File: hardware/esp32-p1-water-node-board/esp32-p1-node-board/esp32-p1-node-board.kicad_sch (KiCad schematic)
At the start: 17 parts, among them J1 RJ11-6, Q1 BC847, Q2 BSS138, U1 TTGO_LoRa32_V11

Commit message: update
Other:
- note added: "GPIO4 zal gebruikt worden als RTS voor de slimmeter"
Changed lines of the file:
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@@
+    (effects (font (size 1.27 1.27)) (justify left bottom))
+  )
+  (text "GPIO4 zal gebruikt worden als RTS voor de slimmeter"
+    (at 208.407 92.583 0)
     (effects (font (size 1.27 1.27)) (justify left bottom))
   )
@@
     (effects (font (size 1.27 1.27)) (justify right bottom))
   )
-  (label "DATA_REQ" (at 40.64 36.83 0)
+  (label "DATA_REQ" (at 40.64 36.83 0) (fields_autoplaced)
     (effects (font (size 1.27 1.27)) (justify left bottom))
   )
-  (label "3V3" (at 111.76 58.42 0)
+  (label "3V3" (at 111.76 58.42 0) (fields_autoplaced)
     (effects (font (size 1.27 1.27)) (justify left bottom))
   )
-  (label "3V3" (at 161.29 58.42 0)
+  (label "3V3" (at 161.29 58.42 0) (fields_autoplaced)
     (effects (font (size 1.27 1.27)) (justify left bottom))
   )
-  (label "3V3" (at 105.41 137.16 180)
+  (label "3V3" (at 105.41 137.16 180) (fields_autoplaced)
     (effects (font (size 1.27 1.27)) (justify right bottom))
   )
-  (label "3V3" (at 59.69 140.97 180)
+  (label "3V3" (at 59.69 140.97 180) (fields_autoplaced)
     (effects (font (size 1.27 1.27)) (justify right bottom))
   )
-  (label "5V" (at 36.83 54.61 0)
+  (label "5V" (at 36.83 54.61 0) (fields_autoplaced)
     (effects (font (size 1.27 1.27)) (justify left bottom))
   )
-  (label "HARD_RXD" (at 73.66 113.03 0)
+  (label "HARD_RXD" (at 73.66 113.03 0) (fields_autoplaced)
     (effects (font (size 1.27 1.27)) (justify left bottom))
   )
-  (label "HARD_RXD" (at 111.76 63.5 0)
+  (label "HARD_RXD" (at 111.76 63.5 0) (fields_autoplaced)
     (effects (font (size 1.27 1.27)) (justify left bottom))
   )
-  (label "DATA" (at 40.64 29.21 0)
+  (label "DATA" (at 40.64 29.21 0) (fields_autoplaced)
     (effects (font (size 1.27 1.27)) (justify left bottom))
   )
-  (label "SOFT_REQ" (at 73.66 137.16 0)
+  (label "SOFT_REQ" (at 73.66 137.16 0) (fields_autoplaced)
     (effects (font (size 1.27 1.27)) (justify left bottom))
   )
-  (label "GND" (at 161.29 53.34 0)
+  (label "GND" (at 161.29 53.34 0) (fields_autoplaced)
     (effects (font (size 1.27 1.27)) (justify left bottom))
   )
-  (label "DATA_GND" (at 40.64 34.29 0)
+  (label "DATA_GND" (at 40.64 34.29 0) (fields_autoplaced)
     (effects (font (size 1.27 1.27)) (justify left bottom))
   )
-  (label "DATA_3V3" (at 105.41 168.91 180)
+  (label "DATA_3V3" (at 105.41 168.91 180) (fields_autoplaced)
     (effects (font (size 1.27 1.27)) (justify right bottom))
   )
-  (label "GND" (at 165.1 138.43 180)
+  (label "GND" (at 165.1 138.43 180) (fields_autoplaced)
     (effects (font (size 1.27 1.27)) (justify right bottom))
   )
-  (label "5V" (at 161.29 55.88 0)
+  (label "5V" (at 161.29 55.88 0) (fields_autoplaced)
     (effects (font (size 1.27 1.27)) (justify left bottom))
   )
-  (label "SOFT_RXD" (at 156.21 73.66 0)
+  (label "SOFT_RXD" (at 156.21 73.66 0) (fields_autoplaced)
     (effects (font (size 1.27 1.27)) (justify left bottom))
   )
-  (label "3V3" (at 77.47 54.61 0)
+  (label "3V3" (at 77.47 54.61 0) (fields_autoplaced)
     (effects (font (size 1.27 1.27)) (justify left bottom))
   )
-  (label "5V" (at 111.76 55.88 0)
+  (label "5V" (at 111.76 55.88 0) (fields_autoplaced)
     (effects (font (size 1.27 1.27)) (justify left bottom))
   )
-  (label "SOFT_REQ" (at 165.1 81.28 180)
+  (label "SOFT_REQ" (at 165.1 81.28 180) (fields_autoplaced)
     (effects (font (size 1.27 1.27)) (justify right bottom))
   )
-  (label "DATA_3V3_N" (at 105.41 161.29 180)
+  (label "DATA_3V3_N" (at 105.41 161.29 180) (fields_autoplaced)
     (effects (font (size 1.27 1.27)) (justify right bottom))
   )
-  (label "SDA" (at 161.29 96.52 0)
+  (label "SDA" (at 161.29 96.52 0) (fields_autoplaced)
     (effects (font (size 1.27 1.27)) (justify left bottom))
   )
-  (label "DATA_3V3_N" (at 83.82 67.31 0)
+  (label "DATA_3V3_N" (at 83.82 67.31 0) (fields_autoplaced)
     (effects (font (size 1.27 1.27)) (justify left bottom))
   )
-  (label "SOFT_TXD" (at 165.1 71.12 180)
+  (label "SOFT_TXD" (at 165.1 71.12 180) (fields_autoplaced)
     (effects (font (size 1.27 1.27)) (justify right bottom))
   )
-  (label "GND" (at 111.76 60.96 0)
+  (label "GND" (at 111.76 60.96 0) (fields_autoplaced)
     (effects (font (size 1.27 1.27)) (justify left bottom))
   )
-  (label "5V" (at 165.1 128.27 180)
+  (label "5V" (at 165.1 128.27 180) (fields_autoplaced)
     (effects (font (size 1.27 1.27)) (justify right bottom))
   )
-  (label "DATA_GND" (at 26.67 87.63 0)
+  (label "DATA_GND" (at 26.67 87.63 0) (fields_autoplaced)
     (effects (font (size 1.27 1.27)) (justify left bottom))
   )
-  (label "DATA_5V_R" (at 38.1 161.29 180)
+  (label "DATA_5V_R" (at 38.1 161.29 180) (fields_autoplaced)
     (effects (font (size 1.27 1.27)) (justify right bottom))
   )
-  (label "SOFT_RXD" (at 105.41 113.03 180)
+  (label "SOFT_RXD" (at 105.41 113.03 180) (fields_autoplaced)
     (effects (font (size 1.27 1.27)) (justify right bottom))
   )
-  (label "DATA_REQ" (at 105.41 144.78 180)
+  (label "DATA_REQ" (at 105.41 144.78 180) (fields_autoplaced)
     (effects (font (size 1.27 1.27)) (justify right bottom))
   )
-  (label "BUTTON" (at 111.76 71.12 0)
+  (label "BUTTON" (at 111.76 71.12 0) (fields_autoplaced)
     (effects (font (size 1.27 1.27)) (justify left bottom))
   )
-  (label "5V" (at 41.91 140.97 180)
+  (label "5V" (at 41.91 140.97 180) (fields_autoplaced)
     (effects (font (size 1.27 1.27)) (justify right bottom))
   )
-  (label "DATA" (at 26.67 73.66 0)
+  (label "DATA" (at 26.67 73.66 0) (fields_autoplaced)
     (effects (font (size 1.27 1.27)) (justify left bottom))
   )
-  (label "GND" (at 83.82 87.63 0)
+  (label "GND" (at 83.82 87.63 0) (fields_autoplaced)
     (effects (font (size 1.27 1.27)) (justify left bottom))
   )
-  (label "DATA_5V_R" (at 53.34 46.99 0)
+  (label "DATA_5V_R" (at 53.34 46.99 0) (fields_autoplaced)
     (effects (font (size 1.27 1.27)) (justify left bottom))
   )
-  (label "RESET" (at 111.76 68.58 0)
+  (label "RESET" (at 111.76 68.58 0) (fields_autoplaced)
     (effects (font (size 1.27 1.27)) (justify left bottom))
   )
-  (label "5V" (at 66.04 54.61 0)
+  (label "5V" (at 66.04 54.61 0) (fields_autoplaced)
     (effects (font (size 1.27 1.27)) (justify left bottom))
   )
-  (label "SCL" (at 111.76 73.66 0)
+  (label "SCL" (at 111.76 73.66 0) (fields_autoplaced)
     (effects (font (size 1.27 1.27)) (justify left bottom))
   )
-  (label "GND" (at 111.76 53.34 0)
+  (label "GND" (at 111.76 53.34 0) (fields_autoplaced)
     (effects (font (size 1.27 1.27)) (justify left bottom))
   )
-  (label "GND" (at 40.64 26.67 0)
+  (label "GND" (at 40.64 26.67 0) (fields_autoplaced)
     (effects (font (size 1.27 1.27)) (justify left bottom))
   )
-  (label "NC" (at 40.64 31.75 0)
+  (label "NC" (at 40.64 31.75 0) (fields_autoplaced)
     (effects (font (size 1.27 1.27)) (justify left bottom))
   )
-  (label "DATA_3V3" (at 105.41 120.65 180)
+  (label "DATA_3V3" (at 105.41 120.65 180) (fields_autoplaced)
     (effects (font (size 1.27 1.27)) (justify right bottom))
   )

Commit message: Update
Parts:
- removed C1: 10n, Capacitor_SMD:C_1206_3216Metric, symbol Device:C
- removed JP1, JP3: Serial-type-select, Jumpers:SMT-JUMPER_3_1-NC_TRACE_SILK, symbol esp32-p1-node-board-rescue:JUMPER-SMT_3_1-NC-SparkFun-Jumpers
- removed JP2: Data-request-select, Jumpers:SMT-JUMPER_3_1-NC_TRACE_SILK, symbol esp32-p1-node-board-rescue:JUMPER-SMT_3_1-NC-SparkFun-Jumpers
- removed Q1: BC847, Package_TO_SOT_SMD:SOT-23, symbol Transistor_BJT:BC847
- removed R3: 12K, Resistor_SMD:R_1206_3216Metric, symbol Device:R
- added D2: BAT54S, Package_TO_SOT_SMD:SOT-23, symbol esp32-p1-node-board-rescue:BAT54S-Diode
- added J2: Conn_01x03, symbol Connector_Generic:Conn_01x03
- added Q1: BSS138, Package_TO_SOT_SMD:SOT-23, symbol Transistor_FET:BSS138
- added U2: ~, symbol my-KiCad-library:TTGO_T3_V1.6.1
- R2: value 1K -> 10K
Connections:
- net 3V3: now also U2.11 (3V3); no longer Q2.1 (G), R5.1, U1.3 (3V3), U1.34 (3V3)
- net 5V: now also D2.2, U2.13 (5V); no longer R1.1, R4.1, U1.2 (5V), U1.35 (5V)
- net HARD_RXD: now also U2.3 (RXD); no longer U1.5 (GPIO03)
- net DATA_P1_3V3: now reaches Q2.2 (S), R5.2
- removed net DATA: J1.5, R1.2, R2.2
- net DATA_5V_R renamed DATA_P1
- net DATA_P1: now also J1.5; no longer R2.1
- removed net DATA_GND: C2.2, C3.1, Conn1.5 (GND), D1.1, J1.3, J1.6, U1.1 (GND), U1.36 (GND), U1.4 (GND)
- net DATA_REQ renamed DATA_P1_REQ
- new net: Q2.1 (G), R5.1
- new net: Q1.1 (G), R2.1
- new net DATA_P1_GND: D1.1, J1.3
- new net GND: C2.2, C3.1, Conn1.5 (GND), J1.6, U2.10 (GND), U2.12 (GND)
- new net PULSE_WATER: D2.3, Q1.3 (D), R1.2
- new net PULSE_WATER_3V3: Q1.2 (S), R2.2
- new net PULSE_WATER_GND: D2.1
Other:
- note removed: "C1 is not required"
- note removed: "LED"
- note removed: "LoRa_CS"
- note removed: "LoRa_IRQ"
- note removed: "LoRa_MISO"
- note removed: "LoRa_MOSI"
- note removed: "LoRa_RST"
- note removed: "LoRa_SCK"
- note removed: "OLED_RST"
- note removed: "OLED_SCL"
- note removed: "OLED_SDA"
- company: (none) -> IoT Apeldoorn
- title: (none) -> IoT-Apeldoorn P1/Watermeter LoRaWAN node
- moved on the sheet: C2, C3, Conn1, D1, Q2, R4, R5, U1

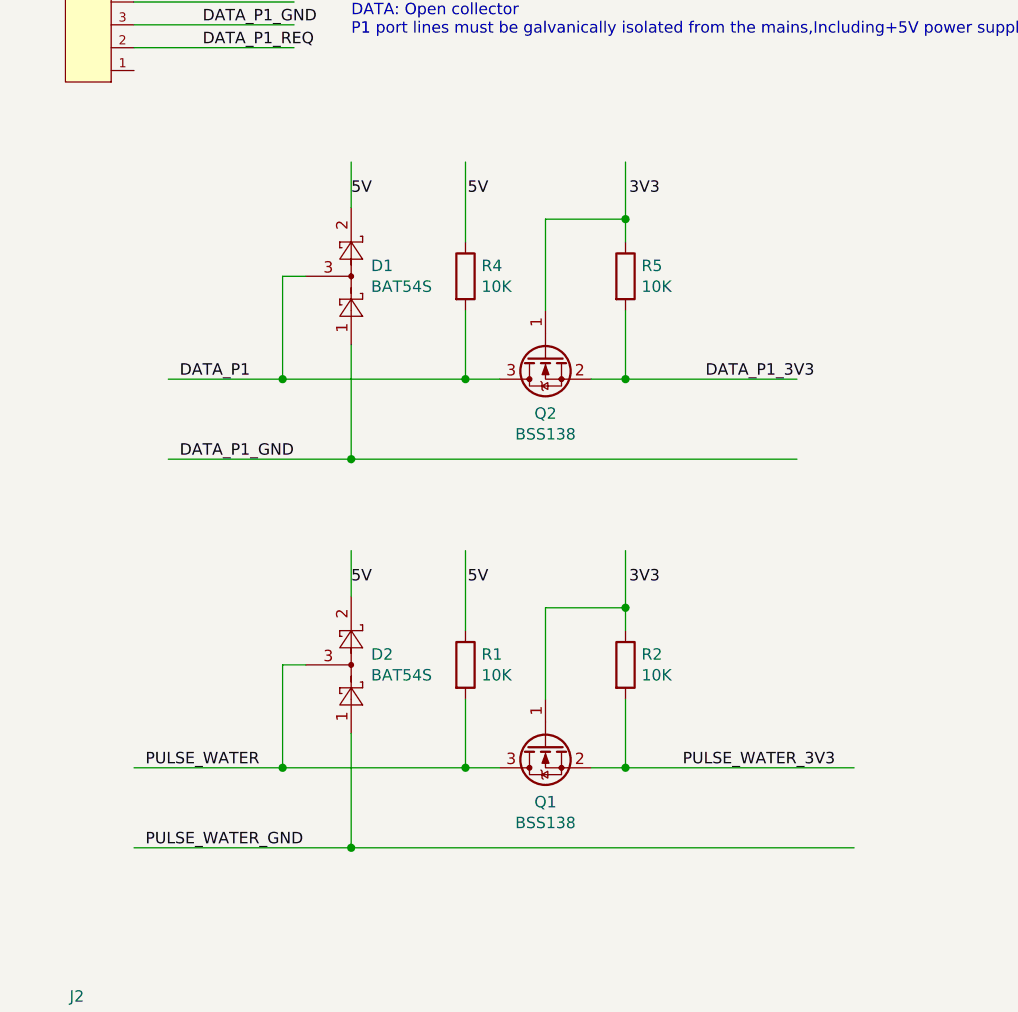
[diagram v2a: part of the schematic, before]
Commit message: Corrections on circuit
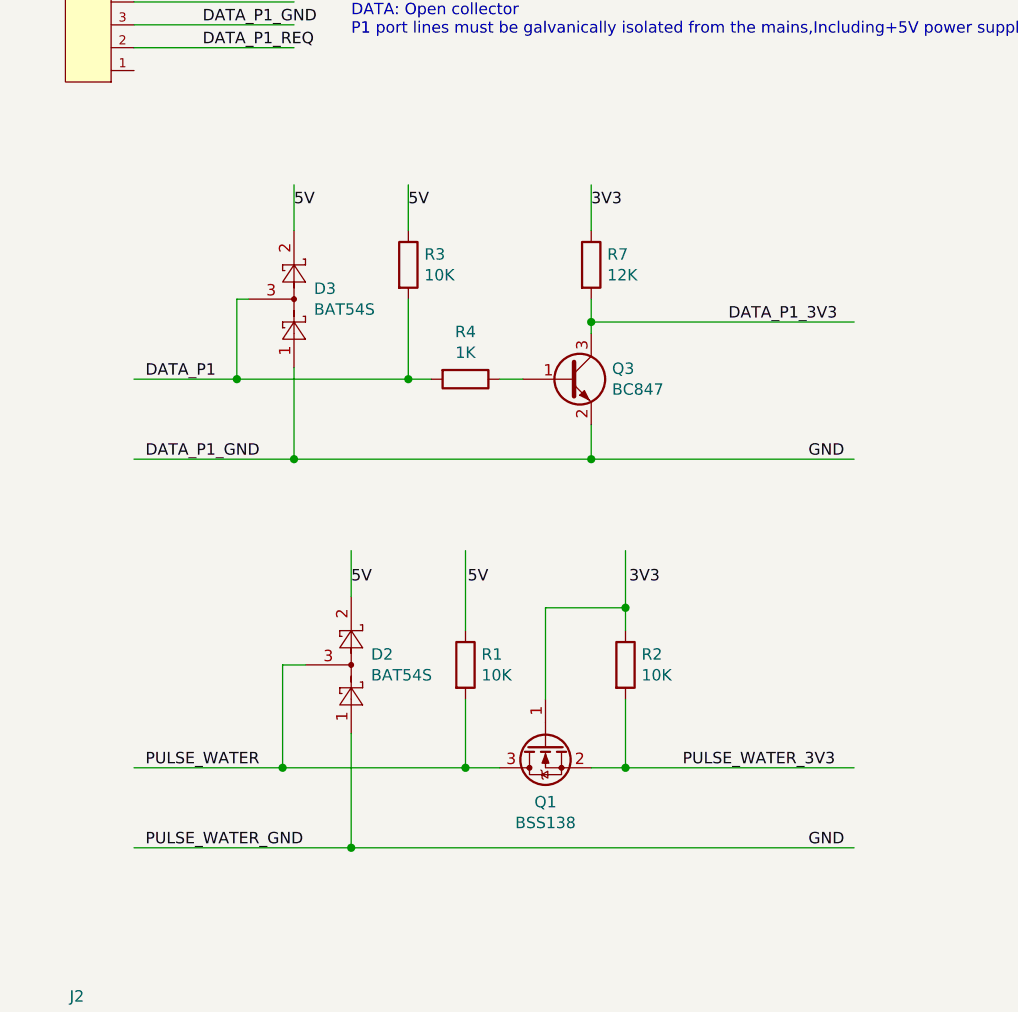
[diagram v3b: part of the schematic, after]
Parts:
- removed D1: BAT54S, Package_TO_SOT_SMD:SOT-23, symbol esp32-p1-node-board-rescue:BAT54S-Diode
- removed Q2: BSS138, Package_TO_SOT_SMD:SOT-23, symbol Transistor_FET:BSS138
- removed R5: 10K, Resistor_SMD:R_1206_3216Metric, symbol Device:R
- added D3: BAT54S, Package_TO_SOT_SMD:SOT-23, symbol esp32-p1-node-board-rescue:BAT54S-Diode
- added Q3: BC847, Package_TO_SOT_SMD:SOT-23, symbol Transistor_BJT:BC847
- added R3: 10K, Resistor_SMD:R_1206_3216Metric, symbol Device:R
- added R7: 12K, Resistor_SMD:R_1206_3216Metric, symbol Device:R
- R4: value 10K -> 1K
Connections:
- net GND is gone; now on net DATA_P1_GND: C2.2, C3.1, Conn1.5 (GND), J1.6, U2.10 (GND), U2.12 (GND)
- net PULSE_WATER_GND is gone; now on net DATA_P1_GND: D2.1
- net 3V3: now also R7.1
- net 5V: now also D3.2, R3.1
- net DATA_P1: now also D3.3, R3.2
- net DATA_P1_3V3: now also Q3.3 (C), R7.2
- net DATA_P1_GND: now also D3.1, Q3.2 (E)
- net at R4.1: now also Q3.1 (B)

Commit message: Update
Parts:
- removed U1: TTGO_LoRa32_V11, esp32-p1-node-board:TTGO_LoRa32_V11, symbol esp32-p1-node-board-rescue:TTGO_LoRa32_V11-esp32_node
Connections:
- net HARD_RXD is gone; now on net DATA_P1_3V3: U2.3 (RXD)
- net 5V: now also J2.1 (Pin_1)
- net DATA_P1_GND: now also J2.3 (Pin_3)
- net DATA_P1_REQ: now also U2.15 (IO04)
- net PULSE_WATER: now also J2.2 (Pin_2)
- net PULSE_WATER_3V3: now also U2.17 (IO02)
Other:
- note added: "BN+ (Brown) = 5V DC BK (Black) = 300 mA pulse BU (Blue) = NPN NO (Ground)"
- moved on the sheet: D2, J2, Q1, R1, R2, U2

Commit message: Updated files to KiCad 8.0
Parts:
- J2: footprint (none) -> Connector_Phoenix_MSTB:PhoenixContact_MSTBA_2,5_3-G_1x03_P5.00mm_Horizontal
- U2: footprint (none) -> my-KiCad-library:TTGO_T3_V1.6.1

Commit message: Start design PCB
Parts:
- removed Q3: BC847, Package_TO_SOT_SMD:SOT-23, symbol Transistor_BJT:BC847
- added C1: 22n, Capacitor_SMD:C_1206_3216Metric, symbol Device:C
- added D1: BAT54S, Package_TO_SOT_SMD:SOT-23, symbol esp32-p1-node-board-rescue:BAT54S-Diode
- added Q2, Q3: BSS138, Package_TO_SOT_SMD:SOT-23, symbol Transistor_FET:BSS138
- added R5, R6, R8, R9: 10K, Resistor_SMD:R_1206_3216Metric, symbol Device:R
- R3: value 10K -> 2K7
- R4: value 1K -> 10K
- R7: value 12K -> 10K
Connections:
- net 3V3: now also Q1.1 (G), R2.1, Q2.1 (G), Q3.1 (G), R5.1
- net 5V: now also R1.1, R4.1, D1.2, R6.1
- net DATA_P1: now also R8.1; no longer R4.2
- net DATA_P1_3V3: now also U2.23 (IO34), Q2.2 (S), R5.2; no longer R7.2, U2.3 (RXD)
- net DATA_P1_GND: now also C1.2, D1.1
- net DATA_P1_REQ: now also D1.3, R9.1; no longer U2.15 (IO04)
- net PULSE_WATER_3V3: now also U2.15 (IO04); no longer U2.17 (IO02)
- net DATA_P1_REQ_3V3: now reaches U2.21 (IO14)
- net DATA_P1_REQ_3V3: now also R7.2, Q3.2 (S)
- new net: C1.1, Q3.3 (D), R6.2, R9.2
- new net: Q2.3 (D), R4.2, R8.2
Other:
- note added: "Mini-USB interface Power"
- note added: "P1 interface"
- note added: "Proximity sensor watermeter"
- note removed: "GPIO4 zal gebruikt worden als RTS voor de slimmeter"
- note removed: "TXD"
- moved on the sheet: C2, C3, Conn1, D2, D3, J1, J2, Q1, R1, R2, R3, U2

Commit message: Final PCB design voor proef
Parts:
- renumbered D3 to D1, D1 to D3, Q2 to Q1, Q1 to Q2, R3 to R1, R8 to R2, R5 to R3, R1 to R5, R9 to R6, R6 to R7, R2 to R8, R7 to R9, U2 to U1
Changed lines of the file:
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@@
 		(on_board yes)
 		(dnp no)
-		(property "Reference" "R6"
+		(property "Reference" "R7"
 			(at 93.218 116.9416 0)
 			(effects
@@
 			(project "esp32-p1-node-board"
 				(path "/01cb7ed1-ac17-4d3b-aabe-b728477810cf"
-					(reference "R6")
+					(reference "R7")
 					(unit 1)
 				)
@@
 		(on_board yes)
 		(dnp no)
-		(property "Reference" "D3"
+		(property "Reference" "D1"
 			(at 68.2498 80.1116 90)
 			(effects
@@
 			(project "esp32-p1-node-board"
 				(path "/01cb7ed1-ac17-4d3b-aabe-b728477810cf"
-					(reference "D3")
+					(reference "D1")
 					(unit 1)
 				)
@@
 		(on_board yes)
 		(dnp no)
-		(property "Reference" "R5"
+		(property "Reference" "R3"
 			(at 110.998 80.1116 0)
 			(effects
@@
 			(project "esp32-p1-node-board"
 				(path "/01cb7ed1-ac17-4d3b-aabe-b728477810cf"
-					(reference "R5")
+					(reference "R3")
 					(unit 1)
 				)
@@
 		(on_board yes)
 		(dnp no)
-		(property "Reference" "R9"
+		(property "Reference" "R6"
 			(at 74.676 129.794 90)
 			(effects
@@
 			(project "esp32-p1-node-board"
 				(path "/01cb7ed1-ac17-4d3b-aabe-b728477810cf"
-					(reference "R9")
+					(reference "R6")
 					(unit 1)
 				)
@@
 		(on_board yes)
 		(dnp no)
-		(property "Reference" "R3"
+		(property "Reference" "R1"
 			(at 77.978 78.8416 0)
 			(effects
@@
 			(project "esp32-p1-node-board"
 				(path "/01cb7ed1-ac17-4d3b-aabe-b728477810cf"
-					(reference "R3")
+					(reference "R1")
 					(unit 1)
 				)
@@
 		(on_board yes)
 		(dnp no)
-		(property "Reference" "R1"
+		(property "Reference" "R5"
 			(at 93.218 157.5816 0)
 			(effects
@@
 			(project "esp32-p1-node-board"
 				(path "/01cb7ed1-ac17-4d3b-aabe-b728477810cf"
-					(reference "R1")
+					(reference "R5")
 					(unit 1)
 				)
@@
 		(on_board yes)
 		(dnp no)
-		(property "Reference" "R7"
+		(property "Reference" "R9"
 			(at 110.998 116.9416 0)
 			(effects
@@
 			(project "esp32-p1-node-board"
 				(path "/01cb7ed1-ac17-4d3b-aabe-b728477810cf"
-					(reference "R7")
+					(reference "R9")
 					(unit 1)
 				)
@@
 		(on_board yes)
 		(dnp no)
-		(property "Reference" "R2"
+		(property "Reference" "R8"
 			(at 110.998 157.5816 0)
 			(effects
@@
 			(project "esp32-p1-node-board"
 				(path "/01cb7ed1-ac17-4d3b-aabe-b728477810cf"
-					(reference "R2")
+					(reference "R8")
 					(unit 1)
 				)
@@
 		(dnp no)
 		(fields_autoplaced yes)
-		(property "Reference" "U2"
+		(property "Reference" "U1"
 			(at 210.82 105.41 0)
 			(effects
@@
 			(project "esp32-p1-node-board"
 				(path "/01cb7ed1-ac17-4d3b-aabe-b728477810cf"
-					(reference "U2")
+					(reference "U1")
 					(unit 1)
 				)
@@
 		(on_board yes)
 		(dnp no)
-		(property "Reference" "Q2"
+		(property "Reference" "Q1"
 			(at 100.33 93.98 90)
 			(effects
@@
 			(project "esp32-p1-node-board"
 				(path "/01cb7ed1-ac17-4d3b-aabe-b728477810cf"
-					(reference "Q2")
+					(reference "Q1")
 					(unit 1)
 				)
@@
 		(on_board yes)
 		(dnp no)
-		(property "Reference" "D1"
+		(property "Reference" "D3"
 			(at 69.5198 116.9416 90)
 			(effects
@@
 			(project "esp32-p1-node-board"
 				(path "/01cb7ed1-ac17-4d3b-aabe-b728477810cf"
-					(reference "D1")
+					(reference "D3")
 					(unit 1)
 				)
@@
 		(on_board yes)
 		(dnp no)
-		(property "Reference" "Q1"
+		(property "Reference" "Q2"
 			(at 100.33 171.45 90)
 			(effects
@@
 			(project "esp32-p1-node-board"
 				(path "/01cb7ed1-ac17-4d3b-aabe-b728477810cf"
-					(reference "Q1")
+					(reference "Q2")
 					(unit 1)
 				)
@@
 		(on_board yes)
 		(dnp no)
-		(property "Reference" "R8"
+		(property "Reference" "R2"
 			(at 82.296 92.964 90)
 			(effects
@@
 			(project "esp32-p1-node-board"
 				(path "/01cb7ed1-ac17-4d3b-aabe-b728477810cf"
-					(reference "R8")
-					(unit 1)
-				)
+					(reference "R2")
+					(unit 1)
+				)
